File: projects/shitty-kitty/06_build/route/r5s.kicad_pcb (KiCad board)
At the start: 4 copper layers, 130 x 75 mm, 82 parts, among them J1 DC-005C-20A 12V, J2 TYPE-C-31-M-12, J3 ELECTRODES INNER, J4 ELECTRODES OUTER, J5 MOTOR NEMA17, J6 ENDSTOP TERM, J8 HOST 1x6, Q1 AOD4185 revpol, SW1 TS-1187A BOOT, SW2 TS-1187A RESET, U1 ESP32-S3-WROOM-1-N8R2, U2 TMC2209-LA-T, U3 MPR121QR2 0x5A, U4 MPR121QR2 0x5B, U5 MPR121QR2 0x5C, U6 MPR121QR2 0x5D, U7 LIS2DH12TR, U8 AP63205WU-7, U9 AMS1117-3.3

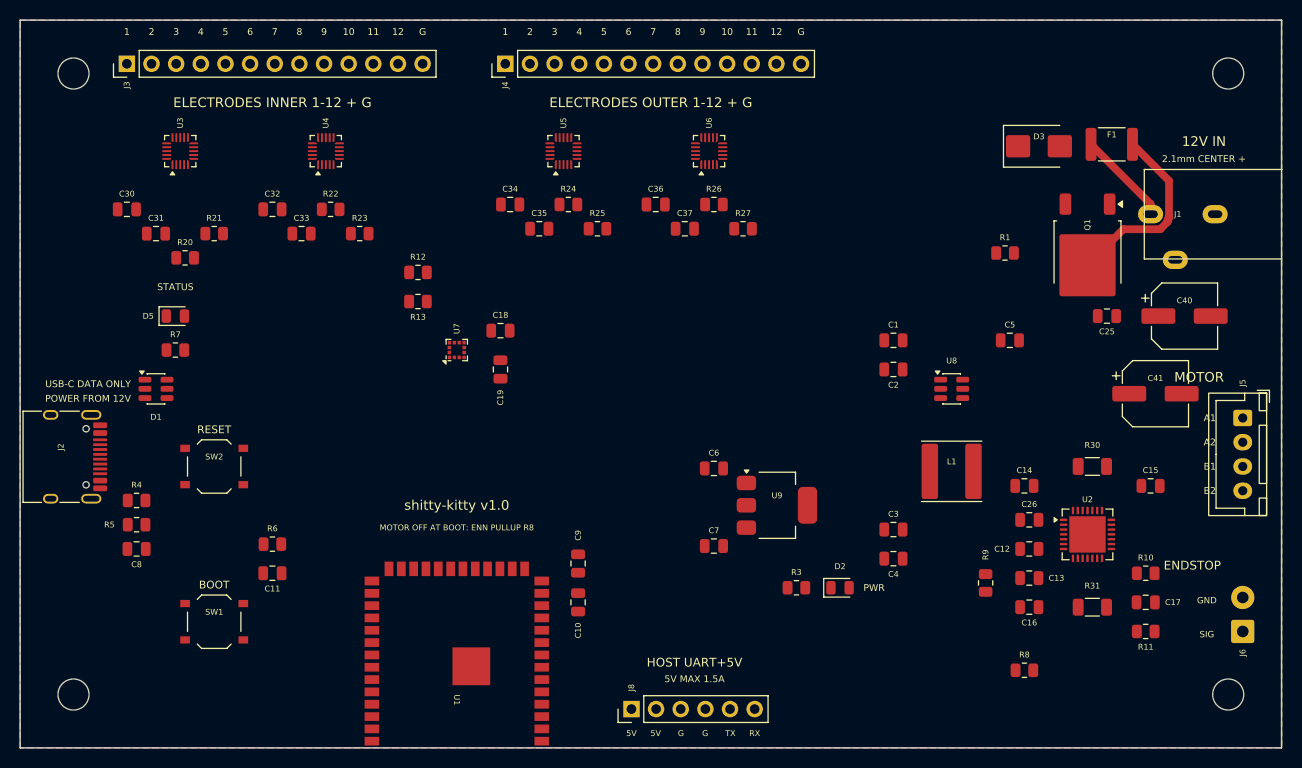
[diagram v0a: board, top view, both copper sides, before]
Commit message: shitty-kitty: fab-floor pin for KRT (no advanced-via escalation), honest hole floors (h2h 0.3/holeclr 0.2), ELEC/3V3 width floors match router grading, route_surgery tool, stitcher fine-pitch GND rescue + via-pad joins
Co-Authored-By: Claude Fable 5 <noreply@anthropic.com>
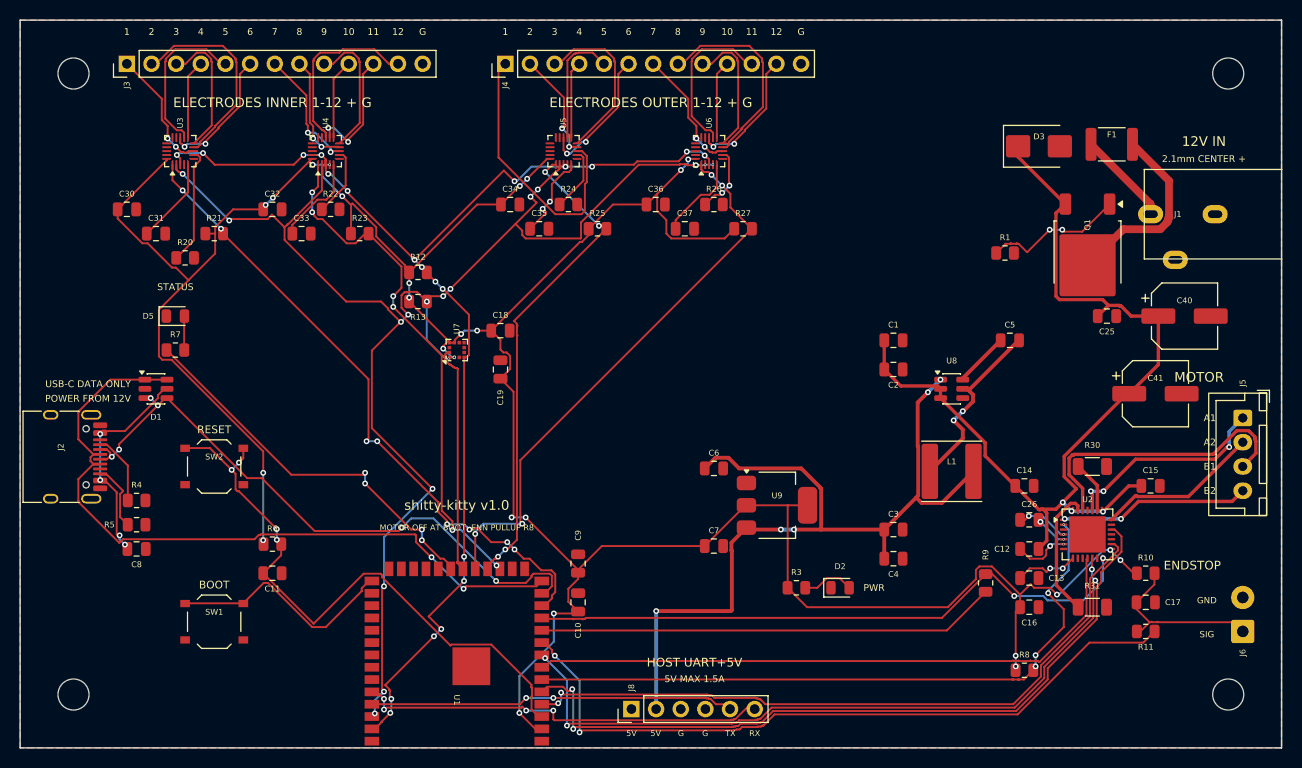
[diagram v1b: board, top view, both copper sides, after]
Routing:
- net 3V3: track 0.00 -> 309.8 mm, vias 0 -> 26
- net SCL: track 0.00 -> 147.1 mm, vias 0 -> 17
- net SDA: track 0.00 -> 125.7 mm, vias 0 -> 21
- net VIN_12V: track 0.00 -> 98.9 mm, vias 0 -> 3
- net 5V: track 0.00 -> 87.8 mm, vias 0 -> 5
- net DIR: track 0.00 -> 77.9 mm, vias 0 -> 2
- net USB_DP: track 0.00 -> 75.6 mm, vias 0 -> 2
- net ENDSTOP_G: track 0.00 -> 74.6 mm, vias 0 -> 2
- net INDEX: track 0.00 -> 74.3 mm, vias 0 -> 4
- net STEP: track 0.00 -> 71.4 mm, vias 0 -> 2
- net ENN: track 0.00 -> 69.0 mm, vias 0 -> 4
- net MPR_IRQ1: track 0.00 -> 67.1 mm, vias 0 -> 8
- net USB_DM: track 0.00 -> 64.7 mm, vias 0 -> 6
- net DIAG: track 0.00 -> 64.5 mm
- net TMC_UART: track 0.00 -> 64.4 mm, vias 0 -> 2
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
